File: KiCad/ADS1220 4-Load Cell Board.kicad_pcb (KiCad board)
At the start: 2 copper layers, 101.6 x 50.8 mm, 84 parts, among them J1 Conn_01x04, J2 Conn_01x04, J3 Conn_01x04, J5 USB_C_Receptacle_USB2.0_14P, J6 Conn_01x02, J7 Conn_01x04, SW1 SW_Push, SW2 SW_Push, U1 STM32F103C8Tx, U2 ADS1220xPW, U3 MCP6V92-E/MS, U4 NCP1117-3.3_SOT223, U5 XPS62912RPUR, Y1 8Mhz

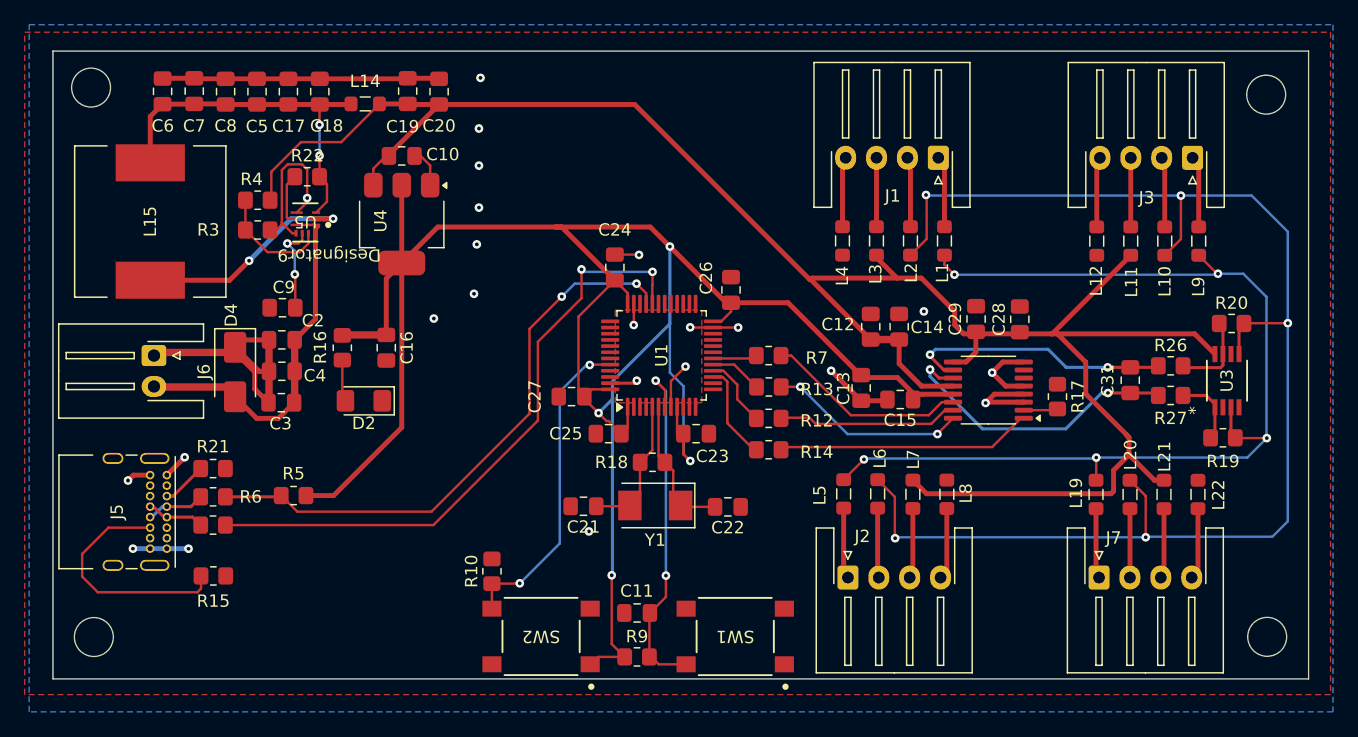
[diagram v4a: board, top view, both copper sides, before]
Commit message: Convert Power to LDOs
Convert power section to use only LDOs. This means we will only get 4.75V or 4.5V on the analog line but this comes with greatly increased simplicity of layout.
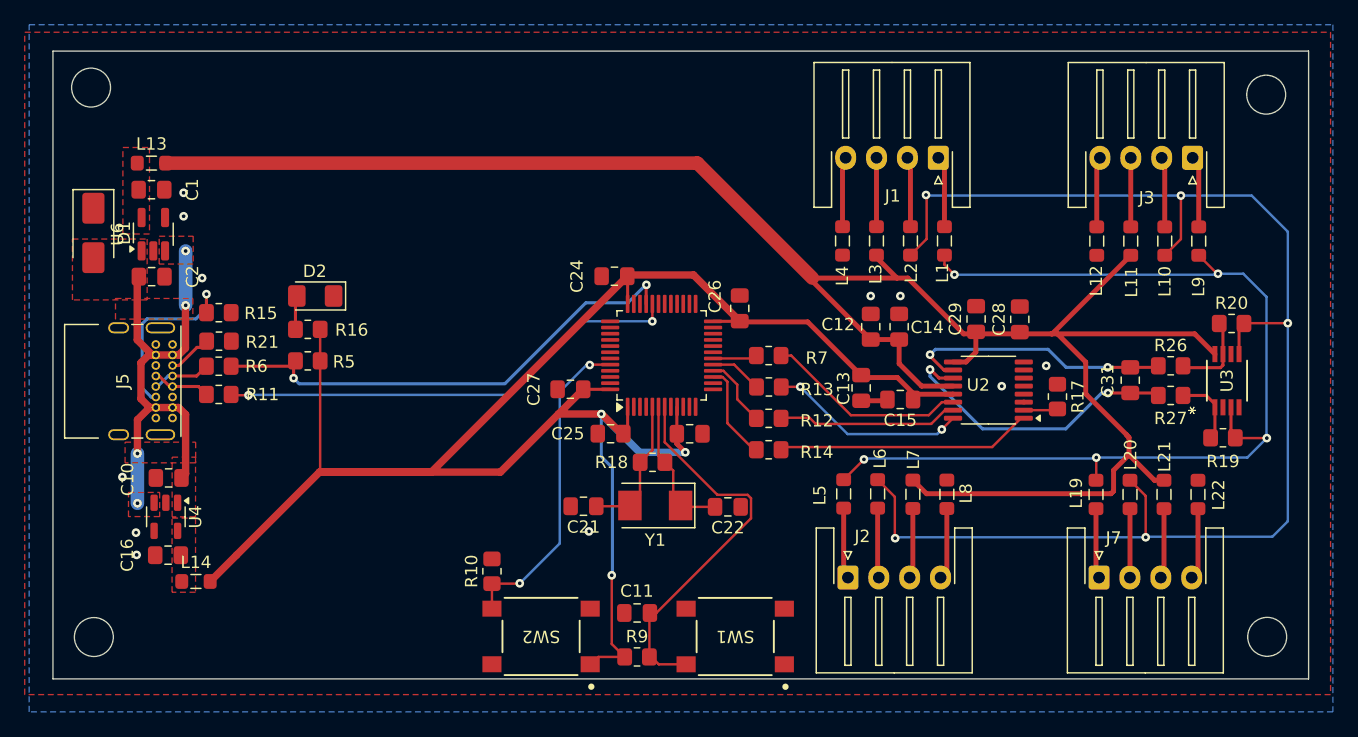
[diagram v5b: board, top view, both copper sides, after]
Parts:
- removed C17, C18, C19, C20, C5, C6, C7, C8: 22uF, Capacitor_SMD:C_0805_2012Metric_Pad1.18x1.45mm_HandSolder
- removed C3, C4: 6.8uF, Capacitor_SMD:C_0805_2012Metric_Pad1.18x1.45mm_HandSolder
- removed C9: 470nF, Capacitor_SMD:C_0805_2012Metric_Pad1.18x1.45mm_HandSolder
- removed D4: SMAJ12A, Diode_SMD:D_SMA
- removed J6: Conn_01x02, Connector_JST:JST_XH_S2B-XH-A-1_1x02_P2.50mm_Horizontal
- removed L15: 2.2uH @ 100mHz 48mOhm, Inductor_SMD:L_Pulse_PA4320
- removed R22: 10k, Resistor_SMD:R_0805_2012Metric_Pad1.20x1.40mm_HandSolder
- removed R3: 25.5k, Resistor_SMD:R_0805_2012Metric_Pad1.20x1.40mm_HandSolder
- removed R4: 4.87k, Resistor_SMD:R_0805_2012Metric_Pad1.20x1.40mm_HandSolder
- removed U5: XPS62912RPUR, TPS62912:RPU0010A-MFG
- added C1: 10uF, Capacitor_SMD:C_0805_2012Metric_Pad1.18x1.45mm_HandSolder, F.Cu at (44.8, 80.0)
- added D1: SMAJ5.0A, Diode_SMD:D_SMA, F.Cu at (40.1, 83.5)
- added L13: 120Ω @ 100MHz / 3A, Inductor_SMD:L_0805_2012Metric_Pad1.05x1.20mm_HandSolder, F.Cu at (44.8, 77.9)
- added U6: TLV702475_SOT23-5, Package_TO_SOT_SMD:SOT-23-5_HandSoldering, F.Cu at (45.0, 83.7)
- C2: value 2.2nF -> 10uF
- L14: value 20Ω @ 100MHz / 5A -> 120Ω @ 100MHz / 3A
- U4: footprint Package_TO_SOT_SMD:SOT-223-3_TabPin2 -> Package_TO_SOT_SMD:SOT-23-5
- moved L14 41.0 mm to (48.4, 111.8)
- moved C10 32.2 mm to (46.2, 103.4), turned to 180 degrees
- moved U4 30.4 mm to (46.0, 106.5)
- moved C16 24.4 mm to (46.1, 109.6), turned to 180 degrees
- moved R15 21.3 mm to (50.2, 90.0)
- moved C2 11.7 mm to (44.8, 87.1), turned to 0 degrees
- moved R5 11.0 mm to (57.5, 93.9)
- moved R11 10.6 mm to (50.2, 96.6)
- moved R6 10.6 mm to (50.2, 94.3)
- moved J5 10.6 mm to (46.5, 92.6)
- moved R21 10.3 mm to (50.3, 92.3)
- moved D2 9.35 mm to (58.0, 88.7)
- moved R16 3.17 mm to (57.5, 91.3), turned to 180 degrees
- moved C26 1.65 mm to (92.4, 89.7)
- moved C24 0.71 mm to (82.3, 87.0), turned to 0 degrees
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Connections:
- C12 pad 2: +5V -> +4V
- C14 pad 2: +5V -> +4V
- C16 pad 1: +3.3V -> Net-(U4-OUT)
- C2 pad 1: +12V -> +5V
- C28 pad 1: +5V -> +4V
- C29 pad 1: +5V -> +4V
- J5 pad A4: unconnected-(J5-VBUS-PadA4)_2 -> +5V
- J5 pad A9: unconnected-(J5-VBUS-PadA4)_3 -> +5V
- J5 pad B4: unconnected-(J5-VBUS-PadA4)_1 -> +5V
- J5 pad B9: unconnected-(J5-VBUS-PadA4) -> +5V
- L11 pad 1: +5V -> +4V
- L14 pad 1: Net-(U5-VO) -> Net-(U4-OUT)
- L14 pad 2: +5V -> +3.3V
- L21 pad 1: +5V -> +4V
- L3 pad 1: +5V -> +4V
- L7 pad 1: +5V -> +4V
- U2 pad 12: +5V -> +4V
- U2 pad 9: +5V -> +4V
- U3 pad 8: +5V -> +4V
- U4 pad 1: GND -> +5V
- U4 pad 2: +3.3V -> GND
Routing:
- net +4V: track 0.00 -> 158.4 mm
- net +5V: track 167.2 -> 39.2 mm, vias 0 -> 4
- net GND: track 103.2 -> 2.05 mm, vias 23 -> 11
- net +12V: track 30.5 -> 0.00 mm
- net Net-(U5-VO): track 29.8 -> 0.00 mm, vias 2 -> 0
- net Net-(U5-SW): track 18.4 -> 0.00 mm, vias 2 -> 0
- net USBDM: track 50.9 -> 37.9 mm
- net +3.3V: track 181.8 -> 172.0 mm, vias 4 -> 3
- net Net-(U5-FB): track 9.37 -> 0.00 mm
- net USBDP: track 47.7 -> 39.6 mm
- net Net-(U5-NR_SS): track 7.31 -> 0.00 mm, vias 2 -> 0
- net Net-(J5-CC2): track 19.5 -> 15.0 mm, vias 0 -> 1
- net Net-(U5-PG): track 4.24 -> 0.00 mm
- net NRESET: track 28.9 -> 31.3 mm, vias 2 -> 0
- net PF0: track 11.5 -> 10.2 mm
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- added copper zone on F.Cu, net +5V
- added copper zone on F.Cu, net Net-(U4-OUT)
- added copper zone on F.Cu, net Net-(U6-OUT)
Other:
- board text added: "*"

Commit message: Add Single Wire Debug
* Add Single Wire Debug (SWD) Tag Connect Connector
* Re-layout of 5V power so the 5V pins connect to a pad directly behind the USB connector
* Add 0R resistors to air gap the 3.3V and 5V power rails for incremental board bringup
* Rotate ADS1220 for cleaner layout
* Remove connections to reference voltage pins, since AVDD/AVSS is a valid reference

fixup

fixup

fixup
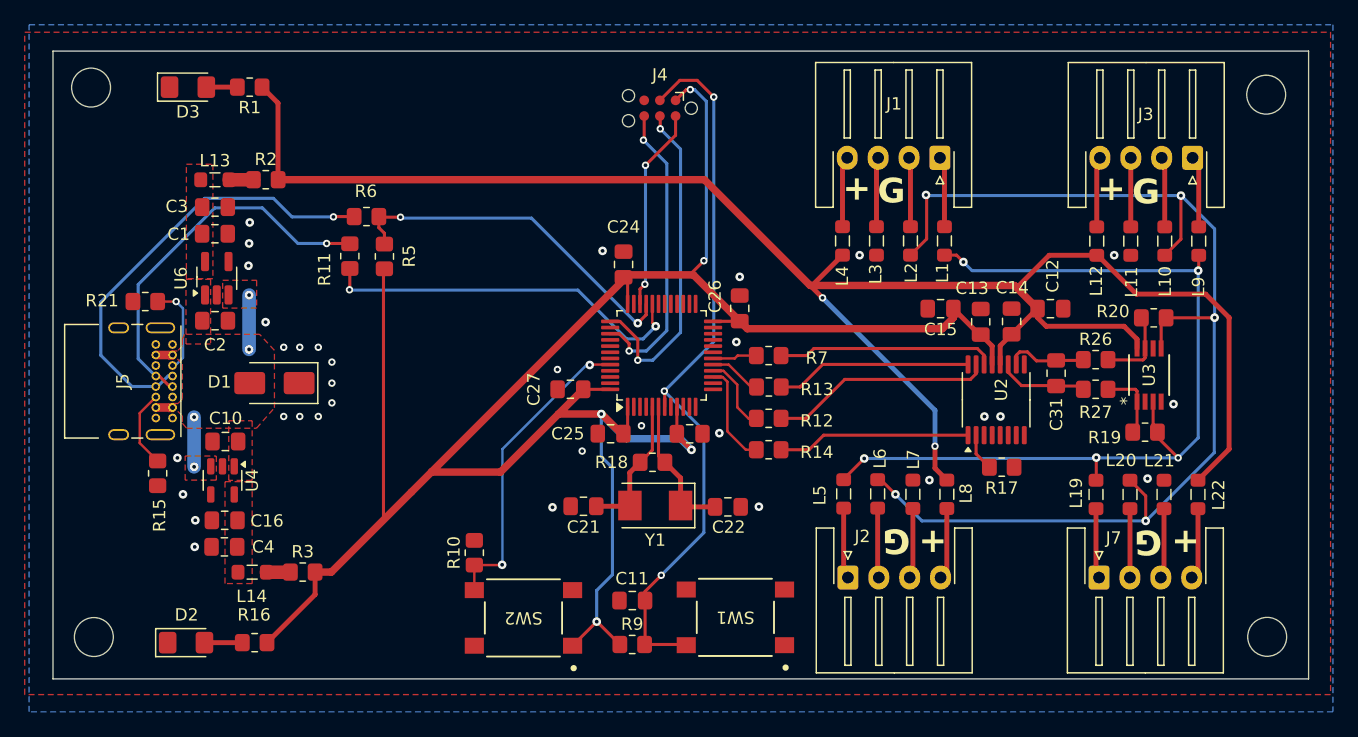
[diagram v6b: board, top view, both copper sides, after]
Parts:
- removed C28: 100n, Capacitor_SMD:C_0805_2012Metric_Pad1.18x1.45mm_HandSolder
- removed C29: 10uF, Capacitor_SMD:C_0805_2012Metric_Pad1.18x1.45mm_HandSolder
- added C3: 10uF, Capacitor_SMD:C_0805_2012Metric_Pad1.18x1.45mm_HandSolder, F.Cu at (49.9, 81.5)
- added C4: 10uF, Capacitor_SMD:C_0805_2012Metric_Pad1.18x1.45mm_HandSolder, F.Cu at (50.7, 109.0)
- added D3: LED, LED_SMD:LED_1206_3216Metric_Pad1.42x1.75mm_HandSolder, F.Cu at (47.8, 71.8)
- added J4: Conn_ARM_SWD_TagConnect_TC2030-NL, Connector:Tag-Connect_TC2030-IDC-NL_2x03_P1.27mm_Vertical, F.Cu at (85.9, 73.5)
- added R1: 1K, Resistor_SMD:R_0805_2012Metric_Pad1.20x1.40mm_HandSolder, F.Cu at (52.8, 71.8)
- added R2: 0R, Resistor_SMD:R_0805_2012Metric_Pad1.20x1.40mm_HandSolder, F.Cu at (54.0, 79.2)
- added R3: 0R, Resistor_SMD:R_0805_2012Metric_Pad1.20x1.40mm_HandSolder, F.Cu at (57.0, 111.0)
- moved D2 29.9 mm to (47.6, 116.7), turned to 0 degrees
- moved R16 25.7 mm to (53.1, 116.7)
- moved D1 19.0 mm to (54.8, 95.7), turned to 180 degrees
- moved R6 17.0 mm to (62.2, 82.2)
- moved R11 15.4 mm to (60.9, 85.4), turned to 90 degrees
- moved C12 14.6 mm to (117.5, 89.7), turned to 180 degrees
- moved R15 13.9 mm to (45.3, 103.0), turned to 90 degrees
- moved C13 11.1 mm to (111.9, 90.7), turned to 90 degrees
- moved R5 10.5 mm to (63.6, 85.5), turned to 90 degrees
- moved C14 9.11 mm to (114.4, 90.7)
- moved C15 8.04 mm to (108.7, 89.7)
- moved R17 7.28 mm to (113.6, 102.5), turned to 180 degrees
- moved R21 6.77 mm to (44.3, 89.1), turned to 0 degrees
- moved R19 6.32 mm to (125.2, 99.7)
- moved U3 6.32 mm to (125.5, 95.0)
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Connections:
- L11 pad 1: +4V -> GND
- L12 pad 1: GND -> +4V
- L13 pad 2: +4V -> Net-(L13-Pad2)
- L14 pad 2: +3.3V -> Net-(L14-Pad2)
- L21 pad 1: +4V -> GND
- L22 pad 1: GND -> +4V
- L3 pad 1: +4V -> GND
- L4 pad 1: GND -> +4V
- L7 pad 1: +4V -> GND
- L8 pad 1: GND -> +4V
- U1 pad 34: unconnected-(U1-PA13-Pad34) -> SWDIO
- U1 pad 37: unconnected-(U1-PA14-Pad37) -> SWCLK
- U1 pad 39: unconnected-(U1-PB3-Pad39) -> SWO
- U2 pad 8: GND -> unconnected-(U2-REFN0-Pad8)
- U2 pad 9: +4V -> unconnected-(U2-REFP0-Pad9)
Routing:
- net Net-(J5-D+-PadA6): track 4.63 -> 36.0 mm, vias 0 -> 1
- net NRESET: track 31.3 -> 59.7 mm, vias 0 -> 3
- net +5V: track 39.2 -> 11.1 mm
- net SWCLK: track 0.00 -> 27.1 mm, vias 0 -> 2
- net Net-(J5-D--PadA7): track 4.71 -> 30.6 mm, vias 0 -> 1
- net SWO: track 0.00 -> 24.4 mm, vias 0 -> 2
- net /Amplifier/AIN1: track 113.6 -> 94.6 mm
- net Net-(U2-AIN0/REFP1): track 23.9 -> 7.28 mm, vias 2 -> 0
- net SWDIO: track 0.00 -> 16.4 mm, vias 0 -> 2
- net Net-(U2-AIN1): track 21.6 -> 6.62 mm, vias 2 -> 0
- net +3.3V: track 172.0 -> 187.0 mm, vias 3 -> 5
- net /Amplifier/AIN0: track 84.4 -> 73.4 mm
- net USBDP: track 39.6 -> 28.8 mm
- net +4V: track 158.4 -> 148.5 mm, vias 0 -> 2
- net Net-(J5-CC2): track 15.0 -> 6.32 mm, vias 1 -> 0
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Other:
- board text added: "+"
- board text added: "G"

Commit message: USB Improvements
* Changed the USB connector symbol and rebuilt it to have pins that match the pads
* Set up the USB lines as a differential pair
* VIA Stitch the board
* Increased minimum trace width to 0.3mm
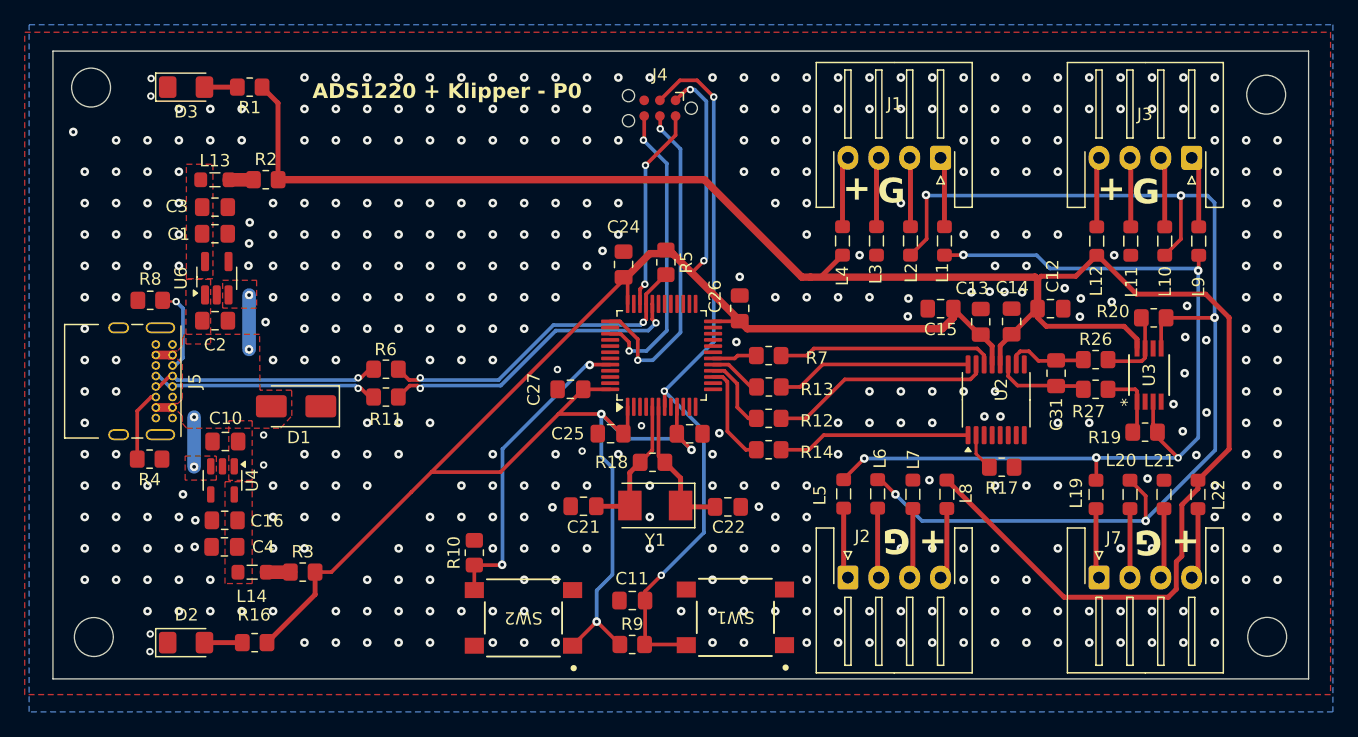
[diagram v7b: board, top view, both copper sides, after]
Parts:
- removed R15, R21: 5.1k, Resistor_SMD:R_0805_2012Metric_Pad1.20x1.40mm_HandSolder
- added R4: 5.1k, Resistor_SMD:R_0805_2012Metric_Pad1.20x1.40mm_HandSolder, F.Cu at (44.6, 101.8)
- added R8: 5.1k, Resistor_SMD:R_0805_2012Metric_Pad1.20x1.40mm_HandSolder, F.Cu at (44.7, 89.0)
- moved R5 22.8 mm to (86.4, 85.9), turned to -90 degrees
- moved R6 12.5 mm to (63.8, 94.6)
- moved R11 11.8 mm to (63.8, 96.8), turned to 180 degrees
- moved D1 2.56 mm to (56.5, 97.6)
- moved D3 0.15 mm to (47.6, 71.8)
- moved J3 0.07 mm to (129.0, 77.5)
- moved J1 0.05 mm to (108.7, 77.5)
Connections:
- net BOOT0_SWCLK renamed BOOT0
- net USBDM renamed /STM32F103C8Tx Microcontroller/USBD-
- net USBDP renamed /STM32F103C8Tx Microcontroller/USBD+
- J5 pad A8: (no net) -> unconnected-(J5-SBU1-PadA8)
- J5 pad B8: (no net) -> unconnected-(J5-SBU2-PadB8)
- J5 pad S1: GND -> (no net)
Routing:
- net +3.3V: track 187.0 -> 162.9 mm
- net Net-(J5-USBDP1): track 36.0 -> 18.5 mm
- net Net-(J5-USBDM1): track 30.6 -> 18.5 mm
- net +4V: track 148.5 -> 159.4 mm, vias 2 -> 0
- net /STM32F103C8Tx Microcontroller/USBD-: track 30.5 -> 25.2 mm
- net /STM32F103C8Tx Microcontroller/USBD+: track 28.8 -> 26.9 mm
- net /Amplifier/AIN1: track 94.6 -> 95.8 mm
- net GND: vias 33 -> 422
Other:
- board text added: "ADS1220 + Klipper - P0"

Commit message: Crystal Changes
* Update crystal selection, schematic and footprint
* Add resistor to limit drive current to crystal
* Block ground plane fill under crystal circuit
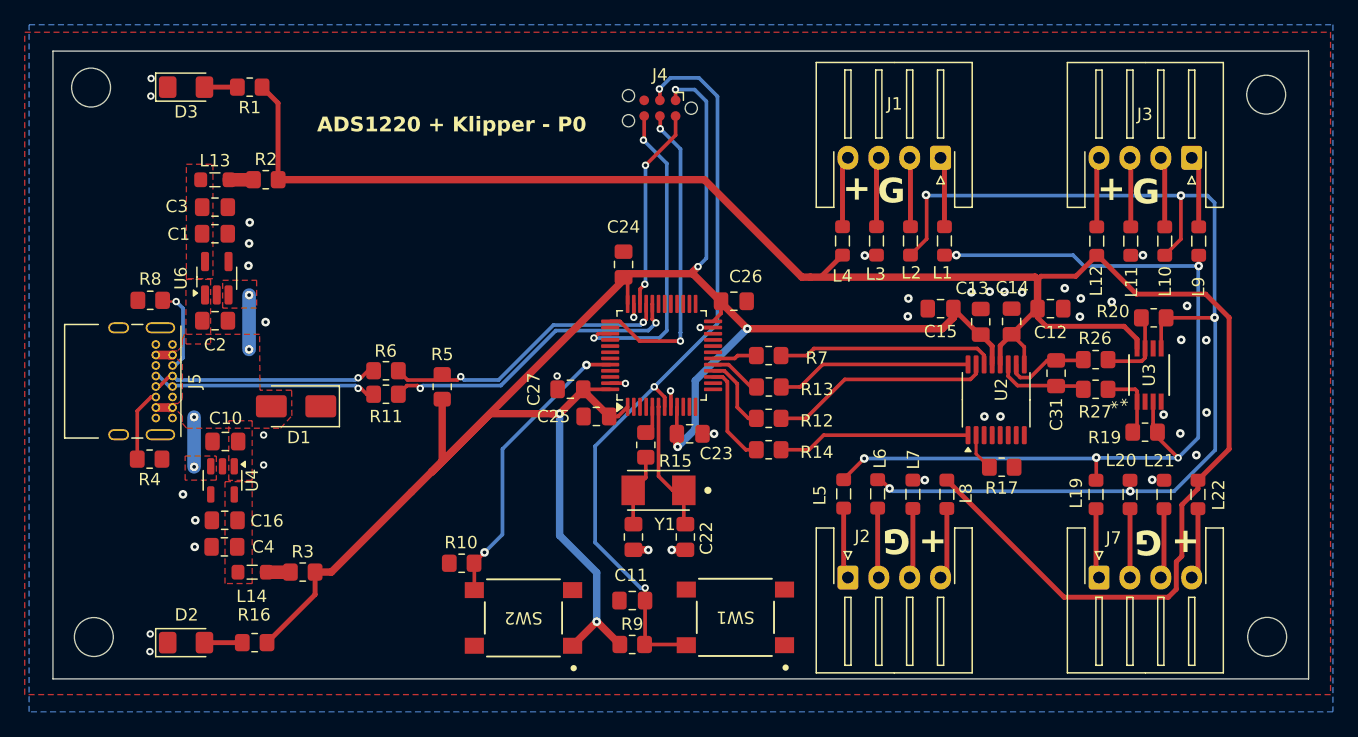
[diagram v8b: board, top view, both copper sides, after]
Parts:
- removed R18: 1M, Resistor_SMD:R_0805_2012Metric_Pad1.20x1.40mm_HandSolder
- added R15: 1.1k, Resistor_SMD:R_0805_2012Metric_Pad1.20x1.40mm_HandSolder, F.Cu at (84.8, 100.7)
- C21, C22: value 10pF -> 18pF
- Y1: footprint Crystal:Crystal_SMD_Abracon_ABM3-2Pin_5.0x3.2mm -> Library:XTAL_ECS-80-18-30-JGN-TR
- moved R5 20.7 mm to (68.3, 96.0), turned to 90 degrees
- moved C21 4.75 mm to (83.8, 108.2), turned to -90 degrees
- moved C22 4.21 mm to (88.0, 108.2), turned to 90 degrees
- moved C25 1.81 mm to (80.8, 98.4)
- moved R10 1.33 mm to (69.9, 110.3), turned to 180 degrees
- moved Y1 1.26 mm to (85.8, 104.4)
- moved C26 0.75 mm to (91.9, 89.1), turned to 180 degrees
- moved R11 0.23 mm to (63.8, 96.6)
- moved R6 0.12 mm to (63.8, 94.7)
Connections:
- net PF1 renamed PD1
- C21 pad 1: PF0 -> Net-(C21-Pad1)
- J5 pad S1: (no net) -> GND
- U1 pad 5: PF0 -> PD0
- U2 pad 8: unconnected-(U2-REFN0-Pad8) -> GND
- U2 pad 9: unconnected-(U2-REFP0-Pad9) -> +4V
- Y1 pad 2: PF0 -> Net-(C21-Pad1)
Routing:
- net PF0: track 11.4 -> 0.00 mm
- net GND: track 0.01 -> 7.00 mm, vias 422 -> 44
- net Net-(C21-Pad1): track 0.00 -> 5.85 mm
- net +3.3V: track 162.9 -> 168.6 mm, vias 5 -> 6
- net /Amplifier/AIN1: track 95.8 -> 90.9 mm
- net /STM32F103C8Tx Microcontroller/USBD+: track 26.9 -> 23.9 mm
- net +4V: track 159.4 -> 162.3 mm
- net NRESET: track 59.7 -> 62.4 mm
- net PD0: track 0.00 -> 2.30 mm
- net SWCLK: track 27.1 -> 25.3 mm
- net SWO: track 24.4 -> 25.8 mm
- net BOOT0: track 25.2 -> 23.9 mm
- net PD1: track 12.2 -> 11.6 mm
